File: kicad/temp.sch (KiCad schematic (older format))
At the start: 10 parts, among them J1 Conn_01x06_Male, J2 Conn_01x02_Female, M1 Motor_DC, Q1 IRF540N, U1 LM7805_TO220, U2 PIC16F684-IP

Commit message: kicad
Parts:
- added J10, J11, J12, J13, J14, J15, J16, J3, J4, J5, J6, J7, J8, J9: Conn_01x01_Female, Connector_PinHeader_2.54mm:PinHeader_1x01_P2.54mm_Vertical, symbol Connector:Conn_01x01_Female
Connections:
- net 5V: now also J15.1 (Pin_1)
- net Earth: now also J16.1 (Pin_1)
- net PGC: now also J1.5 (Pin_5), J4.1 (Pin_1)
- net PGD: now also J3.1 (Pin_1)
- net Vpp: now also J6.1 (Pin_1)
- net Ben10: now reaches U2.10 (C2IN+/AN4/RC0)
- net Ben10: now also J14.1 (Pin_1)
- net Ben11: now reaches U2.11 (RA2/AN2/T0CKI/INT/C1OUT)
- net Ben11: now also J5.1 (Pin_1)
- net Ben2: now reaches U2.2 (RA5/T1CKI/OSC1/CLKIN)
- net Ben2: now also J8.1 (Pin_1)
- net Ben3: now reaches U2.3 (RA4/AN3/~T1G~/OSC2/CLKOUT)
- net Ben3: now also J7.1 (Pin_1)
- net Ben5: now reaches Q1.1 (G), R1.1, U2.5 (P1A/CCP1/RC5)
- net Ben5: now also J9.1 (Pin_1)
- net Ben6: now reaches U2.6 (P1B/C2OUT/RC4)
- net Ben6: now also J10.1 (Pin_1)
- net Ben7: now reaches U2.7 (P1C/AN7/RC3)
- net Ben7: now also J11.1 (Pin_1)
- net Ben8: now reaches U2.8 (P1D/AN6/RC2)
- net Ben8: now also J12.1 (Pin_1)
- net Ben9: now reaches U2.9 (C2IN-/AN5/RC1)
- net Ben9: now also J13.1 (Pin_1)
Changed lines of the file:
@@
 Wire Wire Line
 	3100 3200 3600 3200
+Wire Wire Line
+	4050 4850 4200 4850
+Text GLabel 4500 3600 0    50   Input ~ 0
+Ben11
+Text GLabel 7950 3800 2    50   Input ~ 0
+Ben6
+Text GLabel 7950 3700 2    50   Input ~ 0
+Ben7
+Text GLabel 7950 3600 2    50   Input ~ 0
+Ben8
+Text GLabel 7950 3500 2    50   Input ~ 0
+Ben9
+Text GLabel 7850 3400 2    50   Input ~ 0
+Ben10
+Text GLabel 4500 3900 0    50   Input ~ 0
+Ben2
+Text GLabel 4500 3800 0    50   Input ~ 0
+Ben3
+Wire Wire Line
+	4500 3600 4600 3600
+Wire Wire Line
+	4500 3800 4600 3800
+Wire Wire Line
+	4500 3900 4600 3900
+Wire Wire Line
+	7800 3400 7850 3400
+Wire Wire Line
+	7800 3500 7950 3500
+Wire Wire Line
+	7800 3600 7950 3600
+Wire Wire Line
+	7800 3700 7950 3700
+Wire Wire Line
+	7800 3800 7950 3800
+$Comp
+L Connector:Conn_01x01_Female J3
+U 1 1 5FC215CE
+P 5350 2450
+F 0 "J3" V 5196 2498 50  0000 L CNN
+F 1 "Conn_01x01_Female" V 5287 2498 50  0000 L CNN
+F 2 "Connector_PinHeader_2.54mm:PinHeader_1x01_P2.54mm_Vertical" H 5350 2450 50  0001 C CNN
+F 3 "~" H 5350 2450 50  0001 C CNN
+	1    5350 2450
+	0    1    1    0
+$EndComp
+$Comp
+L Connector:Conn_01x01_Female J4
+U 1 1 5FC21E93
+P 5500 2450
+F 0 "J4" V 5346 2498 50  0000 L CNN
+F 1 "Conn_01x01_Female" V 5437 2498 50  0000 L CNN
+F 2 "Connector_PinHeader_2.54mm:PinHeader_1x01_P2.54mm_Vertical" H 5500 2450 50  0001 C CNN
+F 3 "~" H 5500 2450 50  0001 C CNN
+	1    5500 2450
+	0    1    1    0
+$EndComp
+$Comp
+L Connector:Conn_01x01_Female J5
+U 1 1 5FC221FE
+P 5650 2450
+F 0 "J5" V 5496 2498 50  0000 L CNN
+F 1 "Conn_01x01_Female" V 5587 2498 50  0000 L CNN
+F 2 "Connector_PinHeader_2.54mm:PinHeader_1x01_P2.54mm_Vertical" H 5650 2450 50  0001 C CNN
+F 3 "~" H 5650 2450 50  0001 C CNN
+	1    5650 2450
+	0    1    1    0
+$EndComp
+$Comp
+L Connector:Conn_01x01_Female J6
+U 1 1 5FC22528
+P 5800 2450
+F 0 "J6" V 5646 2498 50  0000 L CNN
+F 1 "Conn_01x01_Female" V 5737 2498 50  0000 L CNN
+F 2 "Connector_PinHeader_2.54mm:PinHeader_1x01_P2.54mm_Vertical" H 5800 2450 50  0001 C CNN
+F 3 "~" H 5800 2450 50  0001 C CNN
+	1    5800 2450
+	0    1    1    0
+$EndComp
+$Comp
+L Connector:Conn_01x01_Female J7
+U 1 1 5FC22939
+P 5950 2450
+F 0 "J7" V 5796 2498 50  0000 L CNN
+F 1 "Conn_01x01_Female" V 5887 2498 50  0000 L CNN
+F 2 "Connector_PinHeader_2.54mm:PinHeader_1x01_P2.54mm_Vertical" H 5950 2450 50  0001 C CNN
+F 3 "~" H 5950 2450 50  0001 C CNN
+	1    5950 2450
+	0    1    1    0
+$EndComp
+$Comp
+L Connector:Conn_01x01_Female J8
+U 1 1 5FC2A7F6
+P 6100 2450
+F 0 "J8" V 5946 2498 50  0000 L CNN
+F 1 "Conn_01x01_Female" V 6037 2498 50  0000 L CNN
+F 2 "Connector_PinHeader_2.54mm:PinHeader_1x01_P2.54mm_Vertical" H 6100 2450 50  0001 C CNN
+F 3 "~" H 6100 2450 50  0001 C CNN
+	1    6100 2450
+	0    1    1    0
+$EndComp
+$Comp
+L Connector:Conn_01x01_Female J9
+U 1 1 5FC2A7FC
+P 6250 2450
+F 0 "J9" V 6096 2498 50  0000 L CNN
+F 1 "Conn_01x01_Female" V 6187 2498 50  0000 L CNN
+F 2 "Connector_PinHeader_2.54mm:PinHeader_1x01_P2.54mm_Vertical" H 6250 2450 50  0001 C CNN
+F 3 "~" H 6250 2450 50  0001 C CNN
+	1    6250 2450
+	0    1    1    0
+$EndComp
+$Comp
+L Connector:Conn_01x01_Female J10
+U 1 1 5FC2A802
+P 6400 2450
+F 0 "J10" V 6246 2498 50  0000 L CNN
+F 1 "Conn_01x01_Female" V 6337 2498 50  0000 L CNN
+F 2 "Connector_PinHeader_2.54mm:PinHeader_1x01_P2.54mm_Vertical" H 6400 2450 50  0001 C CNN
+F 3 "~" H 6400 2450 50  0001 C CNN
+	1    6400 2450
+	0    1    1    0
+$EndComp
+$Comp
+L Connector:Conn_01x01_Female J11
+U 1 1 5FC2A808
+P 6550 2450
+F 0 "J11" V 6396 2498 50  0000 L CNN
+F 1 "Conn_01x01_Female" V 6487 2498 50  0000 L CNN
+F 2 "Connector_PinHeader_2.54mm:PinHeader_1x01_P2.54mm_Vertical" H 6550 2450 50  0001 C CNN
+F 3 "~" H 6550 2450 50  0001 C CNN
+	1    6550 2450
+	0    1    1    0
+$EndComp
+$Comp
+L Connector:Conn_01x01_Female J12
+U 1 1 5FC2A80E
+P 6700 2450
+F 0 "J12" V 6546 2498 50  0000 L CNN
+F 1 "Conn_01x01_Female" V 6637 2498 50  0000 L CNN
+F 2 "Connector_PinHeader_2.54mm:PinHeader_1x01_P2.54mm_Vertical" H 6700 2450 50  0001 C CNN
+F 3 "~" H 6700 2450 50  0001 C CNN
+	1    6700 2450
+	0    1    1    0
+$EndComp
+$Comp
+L Connector:Conn_01x01_Female J13
+U 1 1 5FC2C6D9
+P 6850 2450
+F 0 "J13" V 6696 2498 50  0000 L CNN
+F 1 "Conn_01x01_Female" V 6787 2498 50  0000 L CNN
+F 2 "Connector_PinHeader_2.54mm:PinHeader_1x01_P2.54mm_Vertical" H 6850 2450 50  0001 C CNN
+F 3 "~" H 6850 2450 50  0001 C CNN
+	1    6850 2450
+	0    1    1    0
+$EndComp
+$Comp
+L Connector:Conn_01x01_Female J14
+U 1 1 5FC2C6DF
+P 7000 2450
+F 0 "J14" V 6846 2498 50  0000 L CNN
+F 1 "Conn_01x01_Female" V 6937 2498 50  0000 L CNN
+F 2 "Connector_PinHeader_2.54mm:PinHeader_1x01_P2.54mm_Vertical" H 7000 2450 50  0001 C CNN
+F 3 "~" H 7000 2450 50  0001 C CNN
+	1    7000 2450
+	0    1    1    0
+$EndComp
+$Comp
+L Connector:Conn_01x01_Female J15
+U 1 1 5FC2C6E5
+P 7150 2450
+F 0 "J15" V 6996 2498 50  0000 L CNN
+F 1 "Conn_01x01_Female" V 7087 2498 50  0000 L CNN
+F 2 "Connector_PinHeader_2.54mm:PinHeader_1x01_P2.54mm_Vertical" H 7150 2450 50  0001 C CNN
+F 3 "~" H 7150 2450 50  0001 C CNN
+	1    7150 2450
+	0    1    1    0
+$EndComp
+$Comp
+L Connector:Conn_01x01_Female J16
+U 1 1 5FC2C6EB
+P 7300 2450
+F 0 "J16" V 7146 2498 50  0000 L CNN
+F 1 "Conn_01x01_Female" V 7237 2498 50  0000 L CNN
+F 2 "Connector_PinHeader_2.54mm:PinHeader_1x01_P2.54mm_Vertical" H 7300 2450 50  0001 C CNN
+F 3 "~" H 7300 2450 50  0001 C CNN
+	1    7300 2450
+	0    1    1    0
+$EndComp
+Text GLabel 5350 2250 1    50   Input ~ 0
+PGD
+Text GLabel 5500 2250 1    50   Input ~ 0
+PGC
+Text GLabel 5650 2250 1    50   Input ~ 0
+Ben11
+Text GLabel 5800 2250 1    50   Input ~ 0
+Vpp
+Text GLabel 5950 2250 1    50   Input ~ 0
+Ben3
+Text GLabel 6100 2250 1    50   Input ~ 0
+Ben2
+Text GLabel 8200 3900 3    50   Input ~ 0
+Ben5
+Text GLabel 6250 2250 1    50   Input ~ 0
+Ben5
+Text GLabel 6400 2250 1    50   Input ~ 0
+Ben6
+Text GLabel 6550 2250 1    50   Input ~ 0
+Ben7
+Text GLabel 6700 2250 1    50   Input ~ 0
+Ben8
+Text GLabel 6850 2250 1    50   Input ~ 0
+Ben9
+Text GLabel 7000 2250 1    50   Input ~ 0
+Ben10
+Text GLabel 7150 2250 1    50   Input ~ 0
+5V
+$Comp
+L power:Earth #PWR010
+U 1 1 5FC4537F
+P 7300 2250
+F 0 "#PWR010" H 7300 2000 50  0001 C CNN
+F 1 "Earth" H 7300 2100 50  0001 C CNN
+F 2 "" H 7300 2250 50  0001 C CNN
+F 3 "~" H 7300 2250 50  0001 C CNN
+	1    7300 2250
+	-1   0    0    1
+$EndComp
 $EndSCHEMATC

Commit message: add accel pcb
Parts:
- added C2, C4: C, Capacitor_THT:C_Rect_L7.0mm_W3.5mm_P2.50mm_P5.00mm, symbol Device:C
- added J17, J19, J20, J21: Conn_01x01_Male, Connector_PinHeader_2.54mm:PinHeader_1x01_P2.54mm_Vertical, symbol Connector:Conn_01x01_Male
- added J18: Conn_01x05_Male, Connector_PinHeader_2.54mm:PinHeader_1x05_P2.54mm_Vertical, symbol Connector:Conn_01x05_Male
- added R2, R3: R, Resistor_THT:R_Axial_DIN0207_L6.3mm_D2.5mm_P10.16mm_Horizontal, symbol Device:R
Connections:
- net Earth: now also C2.1, C4.1, J18.4 (Pin_4), J18.5 (Pin_5), J19.1 (Pin_1)
- new net: J17.1 (Pin_1), J18.1 (Pin_1)
- new net: J18.2 (Pin_2), R2.2
- new net: J18.3 (Pin_3), R3.2
- new net: C4.2, J21.1 (Pin_1), R2.1
- new net: C2.2, J20.1 (Pin_1), R3.1
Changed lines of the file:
@@
 	-1   0    0    1
 $EndComp
+$Comp
+L Connector:Conn_01x05_Male J18
+U 1 1 5FCA654C
+P 2450 6500
+F 0 "J18" H 2558 6881 50  0000 C CNN
+F 1 "Conn_01x05_Male" H 2558 6790 50  0000 C CNN
+F 2 "Connector_PinHeader_2.54mm:PinHeader_1x05_P2.54mm_Vertical" H 2450 6500 50  0001 C CNN
+F 3 "~" H 2450 6500 50  0001 C CNN
+	1    2450 6500
+	1    0    0    -1
+$EndComp
+$Comp
+L Device:R R2
+U 1 1 5FCAB6B2
+P 3700 6100
+F 0 "R2" V 3493 6100 50  0000 C CNN
+F 1 "R" V 3584 6100 50  0000 C CNN
+F 2 "Resistor_THT:R_Axial_DIN0207_L6.3mm_D2.5mm_P10.16mm_Horizontal" V 3630 6100 50  0001 C CNN
+F 3 "~" H 3700 6100 50  0001 C CNN
+	1    3700 6100
+	0    1    1    0
+$EndComp
+$Comp
+L Device:R R3
+U 1 1 5FCABBAA
+P 3700 6550
+F 0 "R3" V 3493 6550 50  0000 C CNN
+F 1 "R" V 3584 6550 50  0000 C CNN
+F 2 "Resistor_THT:R_Axial_DIN0207_L6.3mm_D2.5mm_P10.16mm_Horizontal" V 3630 6550 50  0001 C CNN
+F 3 "~" H 3700 6550 50  0001 C CNN
+	1    3700 6550
+	0    1    1    0
+$EndComp
+$Comp
+L Device:C C2
+U 1 1 5FCABEDD
+P 3850 6900
+F 0 "C2" H 3735 6854 50  0000 R CNN
+F 1 "C" H 3735 6945 50  0000 R CNN
+F 2 "Capacitor_THT:C_Rect_L7.0mm_W3.5mm_P2.50mm_P5.00mm" H 3888 6750 50  0001 C CNN
+F 3 "~" H 3850 6900 50  0001 C CNN
+	1    3850 6900
+	-1   0    0    1
+$EndComp
+$Comp
+L Device:C C4
+U 1 1 5FCAC448
+P 4200 6300
+F 0 "C4" H 4085 6254 50  0000 R CNN
+F 1 "C" H 4085 6345 50  0000 R CNN
+F 2 "Capacitor_THT:C_Rect_L7.0mm_W3.5mm_P2.50mm_P5.00mm" H 4238 6150 50  0001 C CNN
+F 3 "~" H 4200 6300 50  0001 C CNN
+	1    4200 6300
+	-1   0    0    1
+$EndComp
+Wire Wire Line
+	3850 6100 4200 6100
+Wire Wire Line
+	4200 6100 4200 6150
+Wire Wire Line
+	3850 6550 3850 6750
+Wire Wire Line
+	2650 6400 3550 6400
+Wire Wire Line
+	3550 6400 3550 6100
+Wire Wire Line
+	2650 6500 3550 6500
+Wire Wire Line
+	3550 6500 3550 6550
+$Comp
+L power:Earth #PWR015
+U 1 1 5FCB1E34
+P 4200 6450
+F 0 "#PWR015" H 4200 6200 50  0001 C CNN
+F 1 "Earth" H 4200 6300 50  0001 C CNN
+F 2 "" H 4200 6450 50  0001 C CNN
+F 3 "~" H 4200 6450 50  0001 C CNN
+	1    4200 6450
+	1    0    0    -1
+$EndComp
+$Comp
+L power:Earth #PWR014
+U 1 1 5FCB24DE
+P 3850 7050
+F 0 "#PWR014" H 3850 6800 50  0001 C CNN
+F 1 "Earth" H 3850 6900 50  0001 C CNN
+F 2 "" H 3850 7050 50  0001 C CNN
+F 3 "~" H 3850 7050 50  0001 C CNN
+	1    3850 7050
+	1    0    0    -1
+$EndComp
+Wire Wire Line
+	3850 6550 4000 6550
+Connection ~ 3850 6550
+Wire Wire Line
+	4200 6100 4450 6100
+Connection ~ 4200 6100
+$Comp
+L Connector:Conn_01x01_Male J20
+U 1 1 5FCB7440
+P 4000 6750
+F 0 "J20" V 4154 6662 50  0000 R CNN
+F 1 "Conn_01x01_Male" V 4063 6662 50  0000 R CNN
+F 2 "Connector_PinHeader_2.54mm:PinHeader_1x01_P2.54mm_Vertical" H 4000 6750 50  0001 C CNN
+F 3 "~" H 4000 6750 50  0001 C CNN
+	1    4000 6750
+	0    -1   -1   0
+$EndComp
+$Comp
+L Connector:Conn_01x01_Male J21
+U 1 1 5FCB9965
+P 4450 6300
+F 0 "J21" V 4604 6212 50  0000 R CNN
+F 1 "Conn_01x01_Male" V 4513 6212 50  0000 R CNN
+F 2 "Connector_PinHeader_2.54mm:PinHeader_1x01_P2.54mm_Vertical" H 4450 6300 50  0001 C CNN
+F 3 "~" H 4450 6300 50  0001 C CNN
+	1    4450 6300
+	0    -1   -1   0
+$EndComp
+Wire Wire Line
+	2750 6600 2650 6600
+$Comp
+L power:Earth #PWR012
+U 1 1 5FCAAA79
+P 2750 6600
+F 0 "#PWR012" H 2750 6350 50  0001 C CNN
+F 1 "Earth" H 2750 6450 50  0001 C CNN
+F 2 "" H 2750 6600 50  0001 C CNN
+F 3 "~" H 2750 6600 50  0001 C CNN
+	1    2750 6600
+	0    -1   -1   0
+$EndComp
+Wire Wire Line
+	2650 6700 2750 6700
+$Comp
+L power:Earth #PWR013
+U 1 1 5FCA8B12
+P 2750 6700
+F 0 "#PWR013" H 2750 6450 50  0001 C CNN
+F 1 "Earth" H 2750 6550 50  0001 C CNN
+F 2 "" H 2750 6700 50  0001 C CNN
+F 3 "~" H 2750 6700 50  0001 C CNN
+	1    2750 6700
+	0    -1   -1   0
+$EndComp
+$Comp
+L Connector:Conn_01x01_Male J19
+U 1 1 5FCBC509
+P 2500 7100
+F 0 "J19" H 2608 7281 50  0000 C CNN
+F 1 "Conn_01x01_Male" H 2608 7190 50  0000 C CNN
+F 2 "Connector_PinHeader_2.54mm:PinHeader_1x01_P2.54mm_Vertical" H 2500 7100 50  0001 C CNN
+F 3 "~" H 2500 7100 50  0001 C CNN
+	1    2500 7100
+	1    0    0    -1
+$EndComp
+$Comp
+L power:Earth #PWR011
+U 1 1 5FCBCC5A
+P 2700 7100
+F 0 "#PWR011" H 2700 6850 50  0001 C CNN
+F 1 "Earth" H 2700 6950 50  0001 C CNN
+F 2 "" H 2700 7100 50  0001 C CNN
+F 3 "~" H 2700 7100 50  0001 C CNN
+	1    2700 7100
+	0    -1   -1   0
+$EndComp
+$Comp
+L Connector:Conn_01x01_Male J17
+U 1 1 5FCBD02D
+P 2450 5950
+F 0 "J17" H 2558 6131 50  0000 C CNN
+F 1 "Conn_01x01_Male" H 2558 6040 50  0000 C CNN
+F 2 "Connector_PinHeader_2.54mm:PinHeader_1x01_P2.54mm_Vertical" H 2450 5950 50  0001 C CNN
+F 3 "~" H 2450 5950 50  0001 C CNN
+	1    2450 5950
+	1    0    0    -1
+$EndComp
+Wire Wire Line
+	2650 6300 2650 5950
 $EndSCHEMATC

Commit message: kortslut modul
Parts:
- added J22: Conn_01x03_Male, Connector_PinHeader_2.54mm:PinHeader_1x03_P2.54mm_Vertical, symbol Connector:Conn_01x03_Male
- added Q2: TIP120, Package_TO_SOT_THT:TO-220-3_Vertical, symbol Transistor_BJT:TIP120
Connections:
- new net: J22.1 (Pin_1), Q2.1 (B)
- new net: J22.3 (Pin_3), Q2.3 (E)
- new net Coll: J22.2 (Pin_2), Q2.2 (C)
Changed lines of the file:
@@
 Wire Wire Line
 	2650 6300 2650 5950
+$Comp
+L Transistor_BJT:TIP120 Q2
+U 1 1 5FCA66AB
+P 1300 4400
+F 0 "Q2" H 1507 4354 50  0000 L CNN
+F 1 "TIP120" H 1507 4445 50  0000 L CNN
+F 2 "Package_TO_SOT_THT:TO-220-3_Vertical" H 1500 4325 50  0001 L CIN
+F 3 "http://www.fairchildsemi.com/ds/TI/TIP120.pdf" H 1300 4400 50  0001 L CNN
+	1    1300 4400
+	-1   0    0    1
+$EndComp
+$Comp
+L Connector:Conn_01x03_Male J22
+U 1 1 5FCA81CF
+P 1900 4400
+F 0 "J22" H 1872 4332 50  0000 R CNN
+F 1 "Conn_01x03_Male" H 1872 4423 50  0000 R CNN
+F 2 "Connector_PinHeader_2.54mm:PinHeader_1x03_P2.54mm_Vertical" H 1900 4400 50  0001 C CNN
+F 3 "~" H 1900 4400 50  0001 C CNN
+	1    1900 4400
+	-1   0    0    1
+$EndComp
+Wire Wire Line
+	1500 4400 1500 4500
+Wire Wire Line
+	1500 4500 1700 4500
+Text GLabel 1200 4600 3    50   Input ~ 0
+Coll
+Text GLabel 1700 4400 0    50   Input ~ 0
+Coll
+Wire Wire Line
+	1200 4200 1700 4200
+Wire Wire Line
+	1700 4200 1700 4300
 $EndSCHEMATC

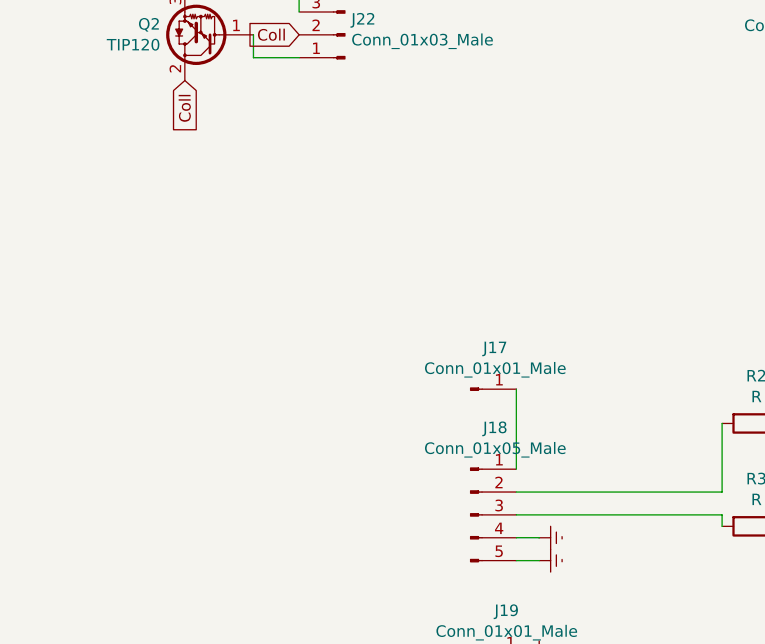
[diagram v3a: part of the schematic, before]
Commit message: 12-3.3V converter
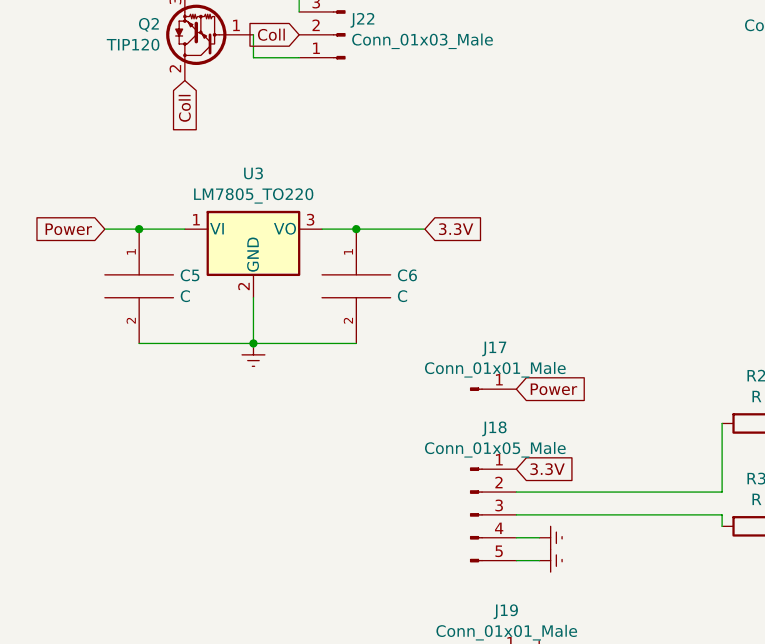
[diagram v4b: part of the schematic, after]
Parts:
- added C5, C6: C, Capacitor_THT:C_Rect_L7.0mm_W3.5mm_P2.50mm_P5.00mm, symbol pspice:C
- added U3: LM7805_TO220, Package_TO_SOT_THT:TO-220-3_Vertical, symbol Regulator_Linear:LM7805_TO220
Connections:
- net Earth: now also C5.2, C6.2, U3.2 (GND)
- net 3.3V: now reaches J18.1 (Pin_1)
- net 3.3V: now also C6.1, U3.3 (VO); no longer J17.1 (Pin_1)
- new net Power: C5.1, J17.1 (Pin_1), U3.1 (VI)
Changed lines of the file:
@@
 	1    0    0    -1
 $EndComp
-Wire Wire Line
-	2650 6300 2650 5950
 $Comp
 L Transistor_BJT:TIP120 Q2
@@
 Wire Wire Line
 	1700 4200 1700 4300
+$Comp
+L Regulator_Linear:LM7805_TO220 U3
+U 1 1 5FD652D0
+P 1500 5250
+F 0 "U3" H 1500 5492 50  0000 C CNN
+F 1 "LM7805_TO220" H 1500 5401 50  0000 C CNN
+F 2 "Package_TO_SOT_THT:TO-220-3_Vertical" H 1500 5475 50  0001 C CIN
+F 3 "https://www.onsemi.cn/PowerSolutions/document/MC7800-D.PDF" H 1500 5200 50  0001 C CNN
+	1    1500 5250
+	1    0    0    -1
+$EndComp
+Wire Wire Line
+	1500 5550 1500 5750
+$Comp
+L pspice:C C6
+U 1 1 5FD652D7
+P 1950 5500
+F 0 "C6" H 2128 5546 50  0000 L CNN
+F 1 "C" H 2128 5455 50  0000 L CNN
+F 2 "Capacitor_THT:C_Rect_L7.0mm_W3.5mm_P2.50mm_P5.00mm" H 1950 5500 50  0001 C CNN
+F 3 "~" H 1950 5500 50  0001 C CNN
+	1    1950 5500
+	1    0    0    -1
+$EndComp
+Wire Wire Line
+	1800 5250 1950 5250
+Wire Wire Line
+	1000 5250 1200 5250
+$Comp
+L pspice:C C5
+U 1 1 5FD652DD
+P 1000 5500
+F 0 "C5" H 1178 5546 50  0000 L CNN
+F 1 "C" H 1178 5455 50  0000 L CNN
+F 2 "Capacitor_THT:C_Rect_L7.0mm_W3.5mm_P2.50mm_P5.00mm" H 1000 5500 50  0001 C CNN
+F 3 "~" H 1000 5500 50  0001 C CNN
+	1    1000 5500
+	1    0    0    -1
+$EndComp
+$Comp
+L power:Earth #PWR016
+U 1 1 5FD738B4
+P 1500 5750
+F 0 "#PWR016" H 1500 5500 50  0001 C CNN
+F 1 "Earth" H 1500 5600 50  0001 C CNN
+F 2 "" H 1500 5750 50  0001 C CNN
+F 3 "~" H 1500 5750 50  0001 C CNN
+	1    1500 5750
+	1    0    0    -1
+$EndComp
+Wire Wire Line
+	1950 5250 2250 5250
+Connection ~ 1950 5250
+Text GLabel 2250 5250 2    50   Input ~ 0
+3.3V
+Text GLabel 2650 6300 2    50   Input ~ 0
+3.3V
+Wire Wire Line
+	1000 5250 850  5250
+Connection ~ 1000 5250
+Text GLabel 850  5250 0    50   Input ~ 0
+Power
+Text GLabel 2650 5950 2    50   Input ~ 0
+Power
+Wire Wire Line
+	1000 5750 1500 5750
+Connection ~ 1500 5750
+Wire Wire Line
+	1950 5750 1500 5750
 $EndSCHEMATC
